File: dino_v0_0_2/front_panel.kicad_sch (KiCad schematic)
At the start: 24 parts

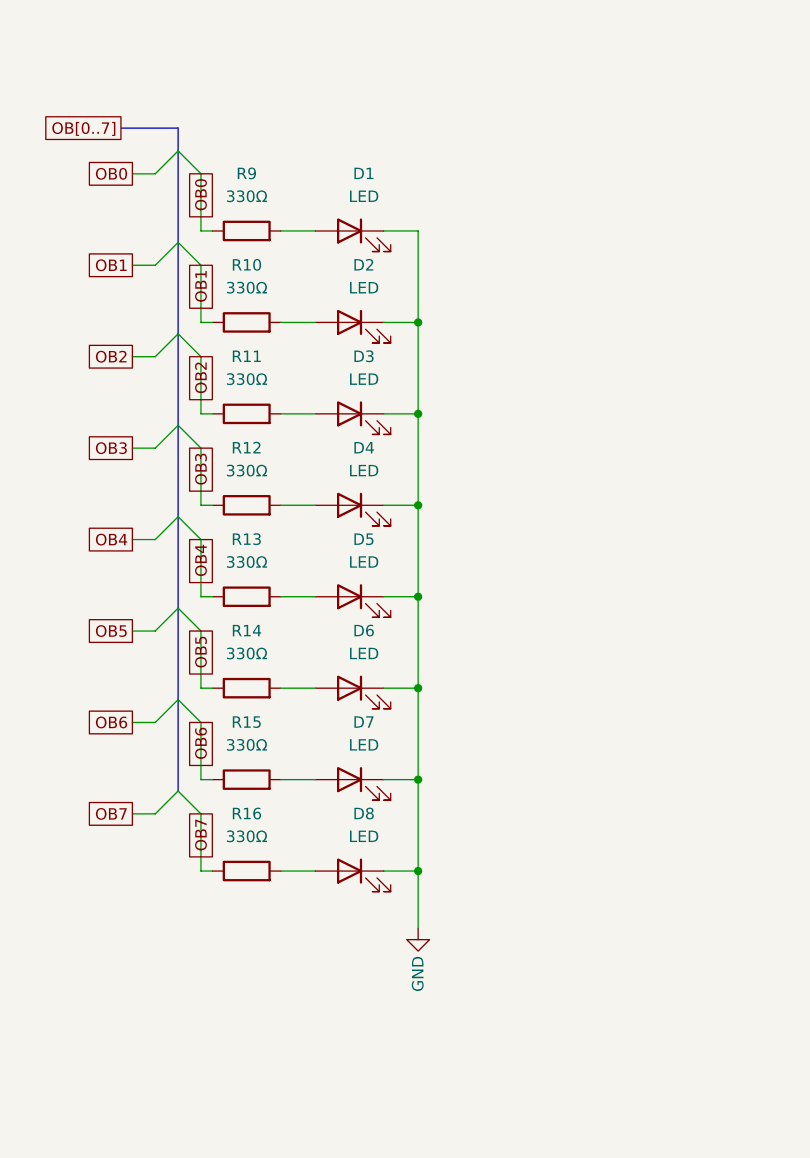
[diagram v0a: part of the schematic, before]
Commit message: feat(pcb): place and route the mainboard, 299x223 2-layer
Draft was 374x524 with nothing routed. Placement by simulated annealing
over a DIP cell grid (HPWL, clock weighted), then hand-trimmed: LEDs and
their 330R leave the board for an OB header J11, W park resistors sit at
the slot-column end, slots J1-J8 respaced to 20.32 mm. Freerouting 2.4.1
on KiCad's own DSN export with the netclasses (Default 0.25, PWR 1.0,
CLK 0.3); GND pours both layers plus router-placed GND bridges. kicad-cli
DRC: 0 unconnected, 0 clearance, 0 shorts; 38 starved-thermal (per-layer
check) and silk warnings remain.

docs/notes/test_pcb_envelope.py enforces the card-edge mechanics against
the saved board: 8 slots in one column at 20.32 mm, no part taller than a
DIP under a card overhang, and CLK/~CLK/CLK_B copper within +20% of the
routed baseline.

Co-Authored-By: Claude Opus 5 <noreply@anthropic.com>
Claude-Session: https://claude.ai/code/session_01Qfuso4zXCFF2iuVHgVo7c8
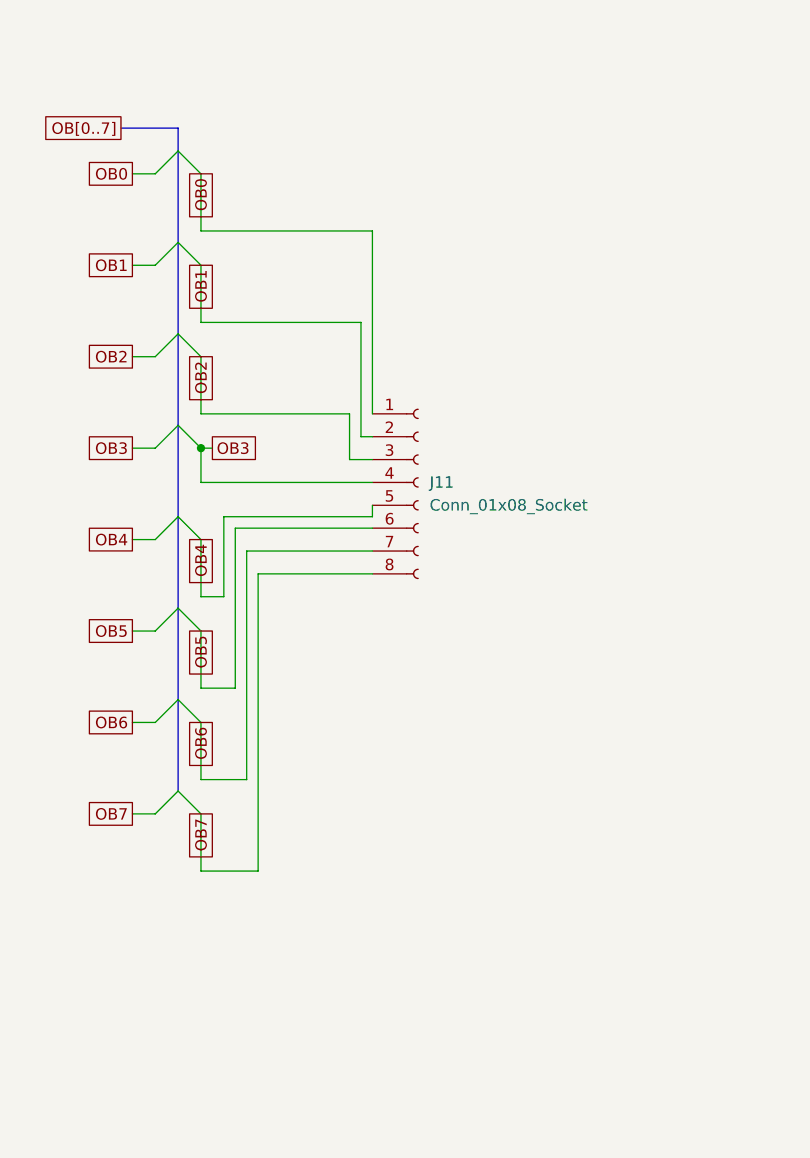
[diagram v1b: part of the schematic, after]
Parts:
- removed D1, D2, D3, D4, D5, D6, D7, D8: LED, LED_THT:LED_D5.0mm, symbol Device:LED
- removed R10, R11, R12, R13, R14, R15, R16, R9: 330Ω, Resistor_THT:R_Axial_DIN0207_L6.3mm_D2.5mm_P10.16mm_Horizontal, symbol Device:R
- added J11: Conn_01x08_Socket, Connector_PinSocket_2.54mm:PinSocket_1x08_P2.54mm_Vertical, symbol Connector:Conn_01x08_Socket
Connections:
- net OB0: now also J11.1 (Pin_1)
- net OB1: now also J11.2 (Pin_2)
- net OB2: now also J11.3 (Pin_3)
- net OB3: now also J11.4 (Pin_4)
- net OB4: now also J11.5 (Pin_5)
- net OB5: now also J11.6 (Pin_6)
- net OB6: now also J11.7 (Pin_7)
- net OB7: now also J11.8 (Pin_8)

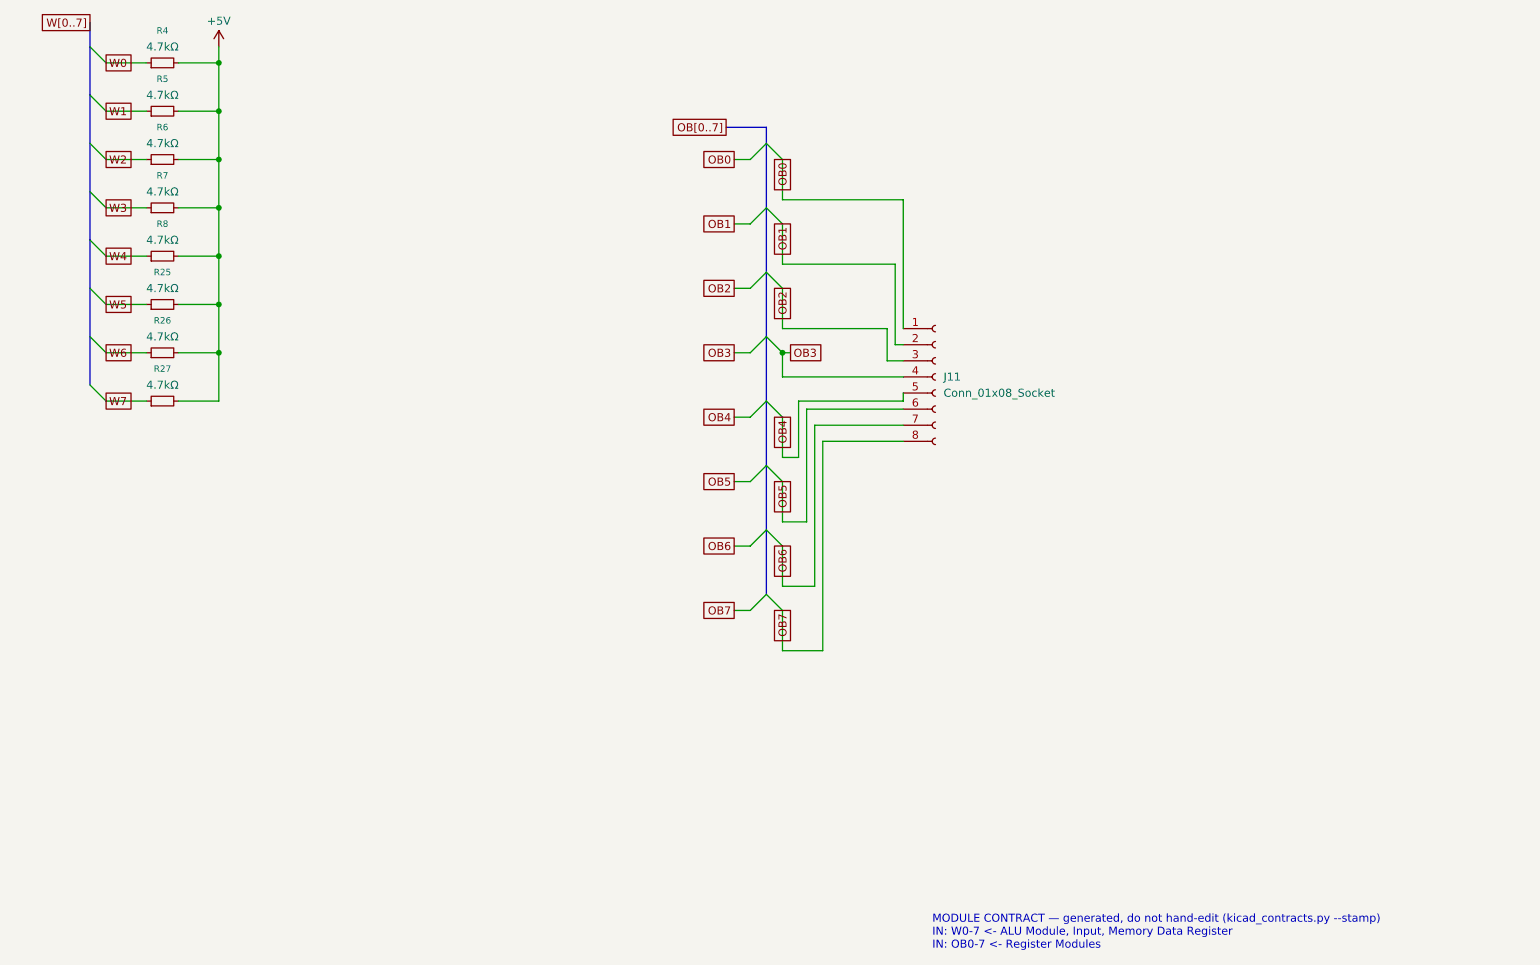
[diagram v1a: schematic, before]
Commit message: feat(int): draw the interrupt block; sheet cleanup pass
New sheet dino_v0_0_2/interrupt.kicad_sch (page 15): U80-U87, R28 4.7k
pull-up on ~{IRQ}, R29 100R on the block's CLK branch, C83-C90. Every
pin per PHASE_INT SECTION 3, checked against the plan with kicad_netlist
and kicad-cli (146 pins, 0 mismatches).

Old sheets (SECTION 3.2): U28.4 lifted off GND to INJECT; U61.3 to
END_OR_ACCEPT; U36.1 to PC_UP_GATED; U49 D0-3 cut from U48 Za-Zd and
routed through U87 as FLAG_NEXT0-3 / FLAG_D0-3; FLAG_C/Z/V/N and the
five decoder outputs made global. dino_serial: U104 74LS05, INTR ->
~{IRQ}, C4.

Placement pass on every sheet: bus entries and global labels no longer
share wires; M, CW, T, IRB and SA buses kept as labelled keys. Nets
diffed against HEAD per sheet: only the intended changes and a rotated
C29. Project ERC: 0 errors. MODULE CONTRACT stamps regenerated.

Co-Authored-By: Claude Fable 5.1 <noreply@anthropic.com>
Claude-Session: https://claude.ai/code/session_01JGxSS4MVUcaZdKZGtKroSg
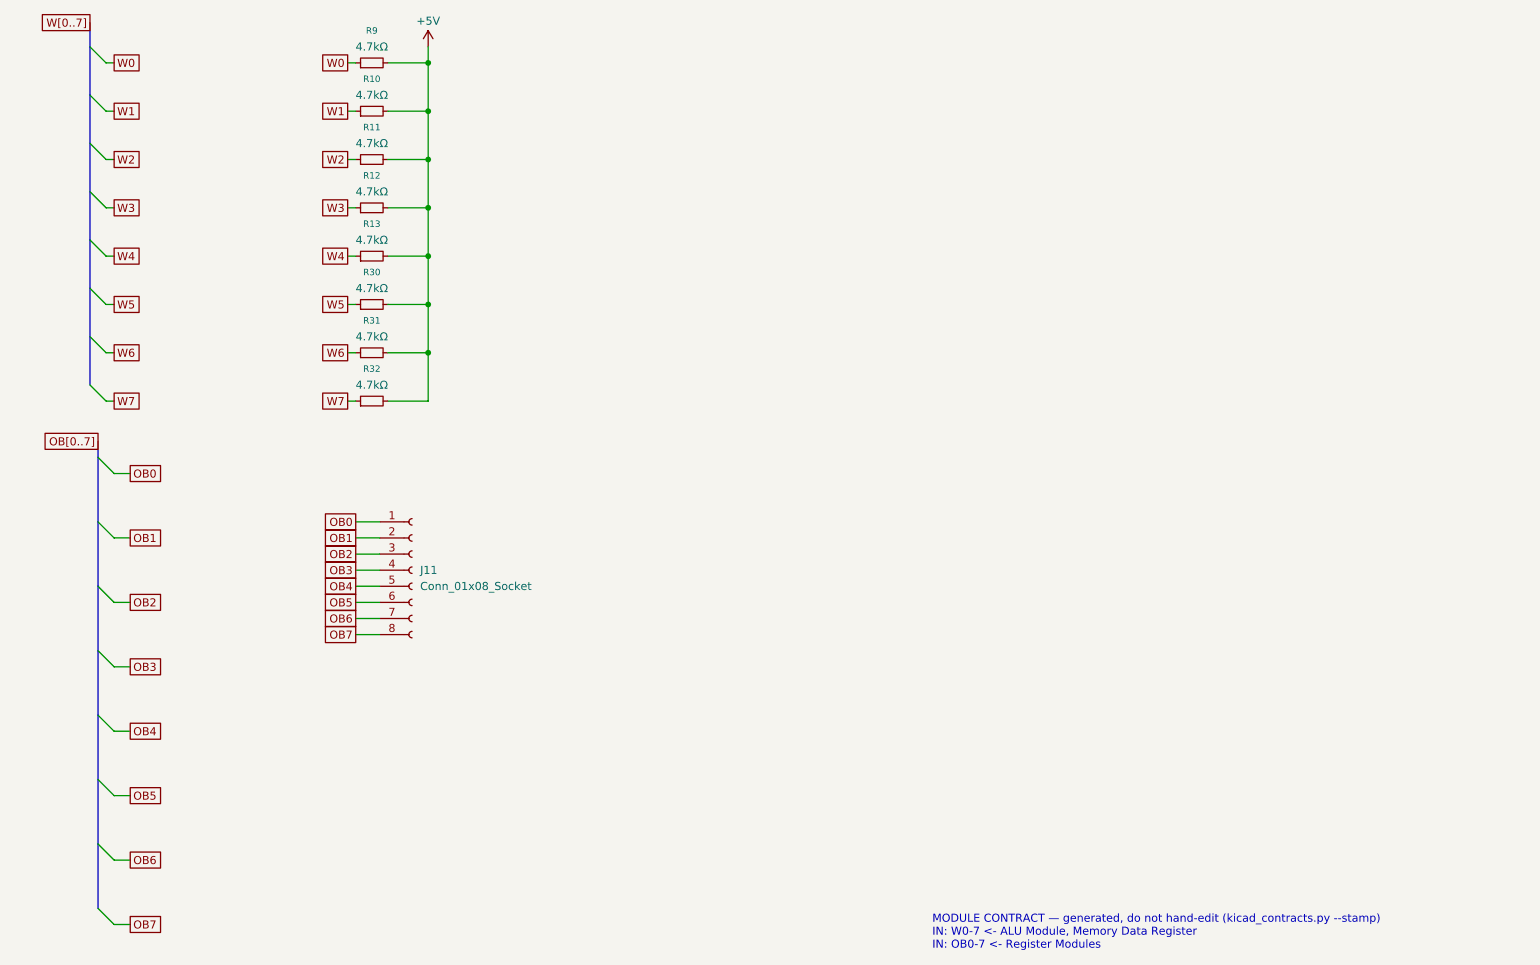
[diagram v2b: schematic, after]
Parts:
- removed R25, R26, R27, R4, R5, R6, R7, R8: 4.7kΩ, Resistor_THT:R_Axial_DIN0207_L6.3mm_D2.5mm_P10.16mm_Horizontal, symbol Device:R_Small
- added R10, R11, R12, R13, R30, R31, R32, R9: 4.7kΩ, Resistor_THT:R_Axial_DIN0207_L6.3mm_D2.5mm_P10.16mm_Horizontal, symbol Device:R_Small
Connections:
- net +5V: now also R10.2, R11.2, R12.2, R13.2, R30.2, R31.2, R32.2, R9.2
- net W0: now also R9.1
- net W1: now also R10.1
- net W2: now also R11.1
- net W3: now also R12.1
- net W4: now also R13.1
- net W5: now also R30.1
- net W6: now also R31.1
- net W7: now also R32.1
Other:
- note added: "MODULE CONTRACT — generated, do not hand-edit (kicad_contracts.py --stamp) IN: W0-7 <- ALU Module, Memory Data Register IN: OB0-7 <- Register Modules"
- note removed: "MODULE CONTRACT — generated, do not hand-edit (kicad_contracts.py --stamp) IN: W0-7 <- ALU Module, Input, Memory Data Register IN: OB0-7 <- Register Modules"
- moved on the sheet: J11

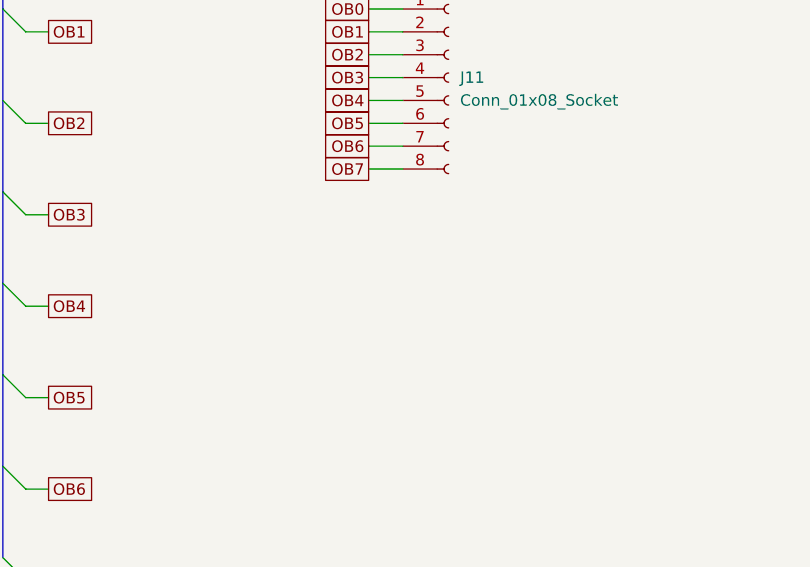
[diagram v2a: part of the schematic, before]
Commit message: feat(pcb): Rev 1.0 pre-order batch, debug access, no fuse
From the five-way pre-order review:

- Debug: J14 clock select at U27.3 (1.024 MHz / 512k / 256k / 128k /
  STEP), STEP debounced from SW3 through the spare U56 5->6 Schmitt;
  J15 LA header (16 control signals, a GND beside each); J16 power for
  the OB LEDs; DNP cap pads C94/C95/C96 on CLK at U6.2, CLK_ALU at
  U47.11 and CW15 (HALT) at U61.5; 15 GND scope loops so every IC but
  two is within 50 mm of one, plus a +5V test point.
- Power: F1 removed, no fuse (Rico); J9's +5V solid to the plane;
  bulk C97-C100 100 uF spread across the board; C92 ceramic.
- Layout: U6 beside U27 (its CLK pin was 138 mm out on raw CLK), C1/R1
  beside U56, RST_SIG in RESET and CLK_R / CLK_INT / CLK_M / CLK_SEL in
  CLK, thermal gap 0.3 mm (GND plane slots from 25 mm to under 8 mm),
  tracks >= 0.2 mm with no neckdown (6/6 mil tier), board min track rule.
- Values to match the bench: U56 SN7414N, U36 74LS00, U51 DM7400N,
  Y1 4.096 MHz.
- Edge socket: silk outline and a pin-1 arrow (unkeyed; a reversed card
  shorts +5V).

Re-routed by Freerouting 2.5.0 from an empty board. KiCad DRC 0
unconnected / 0 errors, schematic parity 0, one text_thickness warning
on the TrueType board text; ERC at its 74 baseline; test_pcb_envelope
7/7. Clock copper: CLK 296 mm, ~{CLK} 283, CLK_B 162, CLK_ALU 48.
Fab: fabrication/dino_rev_1_0_gerbers_20261029_1153.zip.

Co-Authored-By: Claude Opus 5.5 <noreply@anthropic.com>
Claude-Session: https://claude.ai/code/session_01JGxSS4MVUcaZdKZGtKroSg
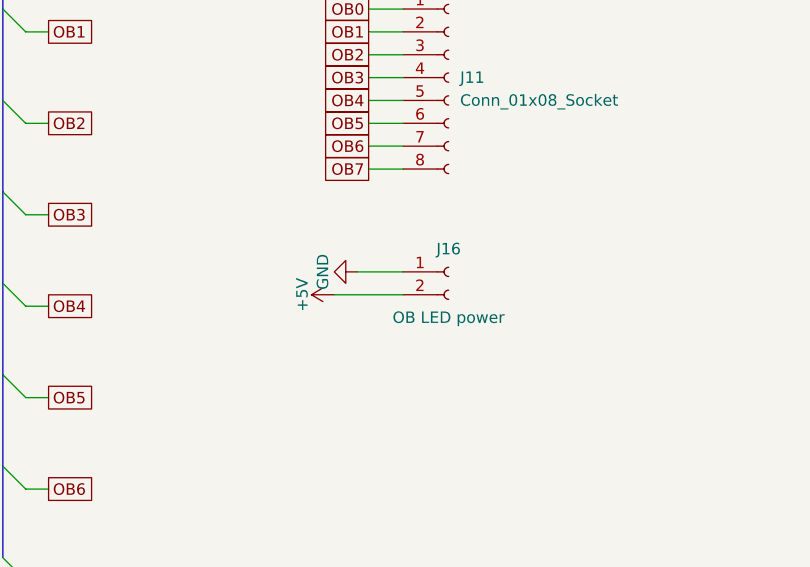
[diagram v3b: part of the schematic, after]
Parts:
- added J16: OB LED power, Connector_PinSocket_2.54mm:PinSocket_1x02_P2.54mm_Vertical, symbol Connector:Conn_01x02_Socket
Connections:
- net +5V: now also J16.2 (Pin_2)
- new net GND: J16.1 (Pin_1)
